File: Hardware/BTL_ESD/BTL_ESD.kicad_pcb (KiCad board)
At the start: 2 copper layers, 73.5 x 92.9 mm, 146 parts, among them J1 DC-005-5A-2.0, J2 BOOT, J3 Load Program, J4 Socket_TFT_1, J5 Socket_TFT_2, J6 USB_B_Micro, J7 220VAC, K1 SRD-05VDC-SL-C, Q1 MMBT2222A, Q2 MMBT2222A, Q3 MMBT2222A, Q4 MMBT2222A, SW1 MS-22D18G2ROHS, SW2 RESET, SW3 ENABLE, SW4 FLASH, U1 ICL7662CBA-T, U2 AMS1117-3.3, U3 TPS54331D, U4 STM32F103RCTx, U5 ESP32-WROOM-32E__4MB_HIGH_TEM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, U6 MCP6002-E_SN, U7 INA128UA, U8 CH340C, U9 PC817, Y1 8MHz, Y2 32.768KHz

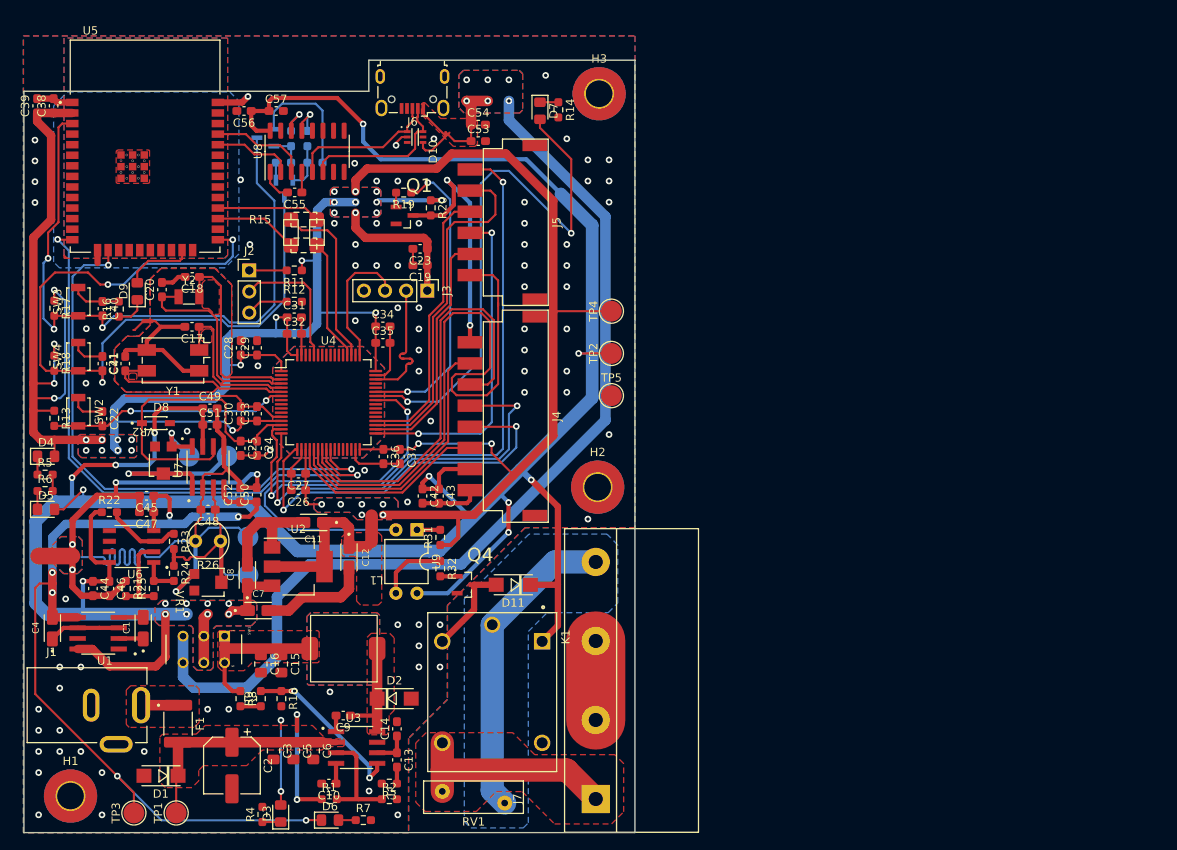
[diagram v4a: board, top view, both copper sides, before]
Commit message: code:ESP32: update uart driver, main.c && hardware file pcb
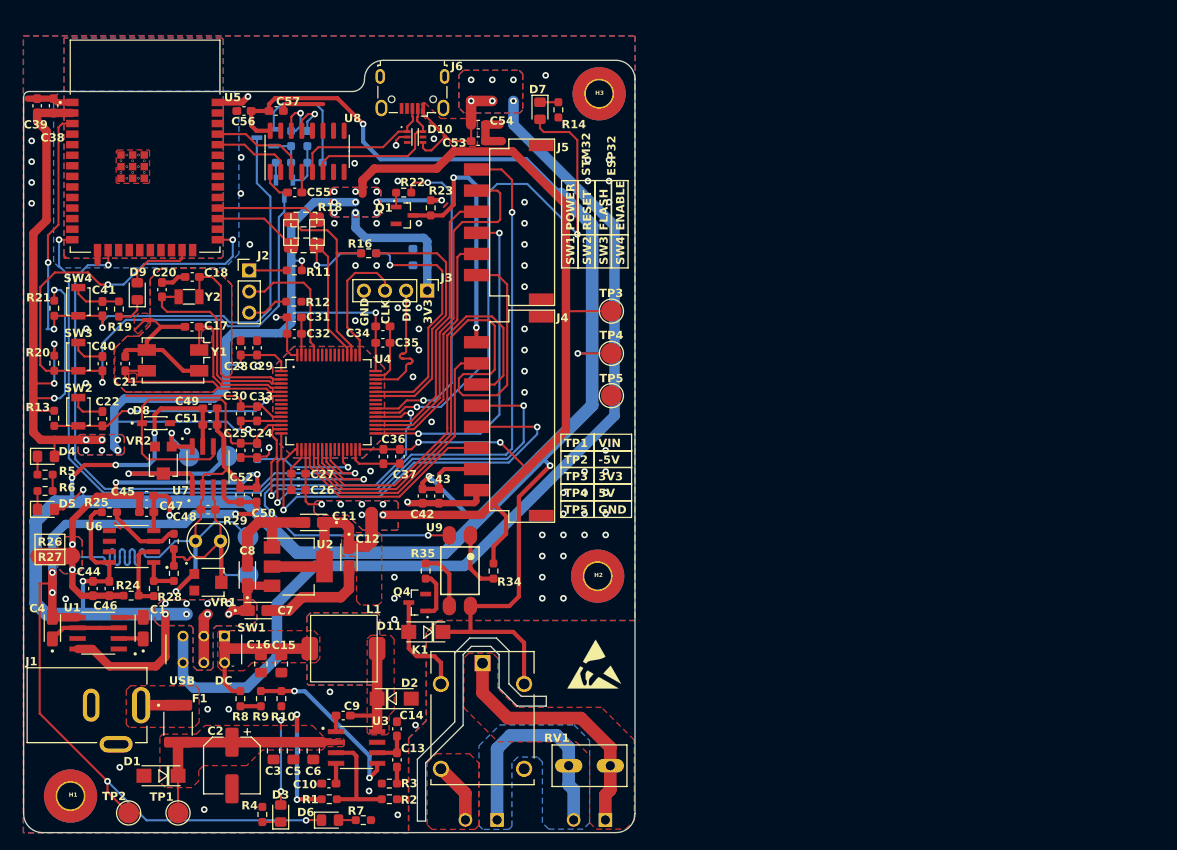
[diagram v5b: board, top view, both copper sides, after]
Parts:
- removed J7: 220VAC, HB9500:HB9500_9_5_4P
- added R15: 0/1%, Resistor_SMD:R_0603_1608Metric_Pad0.98x0.95mm_HandSolder, B.Cu at (139.1, 67.7)
- added R16: 0/1%, Resistor_SMD:R_0603_1608Metric_Pad0.98x0.95mm_HandSolder, F.Cu at (139.1, 67.7)
- added R17: 10k/1%, Resistor_SMD:R_0603_1608Metric_Pad0.98x0.95mm_HandSolder, B.Cu at (125.8, 91.6)
- added REF**: ESD-Logo_6.6x6mm_SilkScreen, Symbol:ESD-Logo_6.6x6mm_SilkScreen, F.Cu at (166.3, 117.1)
- added REF**: ESD-Logo_6.6x6mm_SilkScreen, Symbol:ESD-Logo_6.6x6mm_SilkScreen, B.Cu at (152.8, 127.5)
- added XA1: LED, MKDS1_2-3:PHOENIX_MKDS1_2-3.81, F.Cu at (152.7, 135.9)
- added XA2: 220VAC, MKDS1_2-3:PHOENIX_MKDS1_2-3.81, F.Cu at (165.7, 135.9)
- C19, C23: moved to B.Cu
- K1: value SRD-05VDC-SL-C -> SRA-05VDC-CL; footprint SRD-05VDC-SL-C:RELAY_SRD-05VDC-SL-C -> SRA-05VDC-CL:RELAY_SRA-05VDC-CL
- RV1: value 470V -> MOV-07D471K; footprint Varistor:RV_Disc_D12mm_W3.9mm_P7.5mm -> MOV-14D471K:MOV07D471K
- U9: value PC817 -> PC817X2NIPW; footprint Package_DIP:DIP-4_W7.62mm -> PC817X2NIP0F:SOT254P975X400-4N
- moved RV1 18.0 mm to (165.7, 129.3)
- moved D11 11.9 mm to (146.0, 113.3)
- moved H2 10.7 mm to (166.7, 106.6)
- moved R34 7.57 mm to (154.2, 105.9), turned to -90 degrees
- moved U9 7.12 mm to (150.1, 105.9)
- moved Q4 6.20 mm to (145.0, 109.7), turned to 180 degrees
- moved K1 3.34 mm to (152.8, 123.6)
- moved R35 1.77 mm to (146.0, 105.9)
- moved R24 1.06 mm to (110.6, 108.9), turned to 0 degrees
- moved J4 0.76 mm to (153.7, 87.3)
- moved J5 0.76 mm to (153.7, 64.0)
- moved TP2 0.64 mm to (110.3, 135.0)
- moved C24 0.25 mm to (125.7, 91.4)
- moved C25 0.25 mm to (123.8, 91.4)
- moved TP1 0.23 mm to (116.2, 135.0)
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- renumbered C41 to C40, C40 to C41, R15 to R18, R16 to R19, R18 to R20, R17 to R21, R19 to R22, R20 to R23, R21 to R24, R22 to R25, R23 to R26, R24 to R27, R25 to R28, R26 to R29, R27 to R30, R28 to R31, R29 to R32, R30 to R33, R31 to R34, R32 to R35, SW4 to SW3, SW3 to SW4, TP3 to TP2, TP4 to TP3, TP2 to TP4
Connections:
- net /STM32/BOOT renamed /STM32/BOOT0
- K1 pad NO: Net-(J7-Pin_1) -> Net-(K1-PadNO)
- RV1 pad 1: Net-(J7-Pin_1) -> Net-(RV1-Pad1)
- U4 pad 28: unconnected-(U4-PB2-Pad28) -> Net-(U4-PB2)
- U4 pad 37: unconnected-(U4-PC6-Pad37) -> CONTROL_LED
- U4 pad 38: unconnected-(U4-PC7-Pad38) -> /STM32/LED_TEST
- U4 pad 39: unconnected-(U4-PC8-Pad39) -> TFT_BL
- U4 pad 41: CONTROL_LED -> unconnected-(U4-PA8-Pad41)
- U4 pad 42: /STM32/LED_TEST -> Net-(U4-PA9)
- U4 pad 43: TFT_BL -> Net-(U4-PA10)
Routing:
- net Net-(U4-PA9): track 0.00 -> 31.2 mm
- net Net-(U4-PA10): track 0.00 -> 30.0 mm, vias 0 -> 1
- net Net-(RV1-Pad1): track 0.00 -> 27.4 mm
- net Net-(J7-Pin_1): track 25.7 -> 0.00 mm
- net GND: track 126.5 -> 141.6 mm, vias 83 -> 77
- net Net-(U4-PB2): track 0.00 -> 13.7 mm, vias 0 -> 1
- net Net-(J7-Pin_2): track 9.50 -> 0.00 mm
- net UART4_RX: track 14.7 -> 23.0 mm, vias 0 -> 1
- net +3V3: track 369.2 -> 377.1 mm, vias 35 -> 33
- net Net-(K1-PadNO): track 0.00 -> 7.36 mm
- net Net-(K1-PadCOM): track 37.6 -> 30.6 mm
- net CONTROL_LED: track 47.0 -> 53.7 mm, vias 1 -> 2
- net Net-(U9-A): track 2.79 -> 7.26 mm
- net Net-(Q4-Pad1): track 2.03 -> 5.89 mm
- net TFT_BL: track 36.3 -> 39.7 mm
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- added copper zone on F.Cu, net Net-(K1-PadCOM)
- added copper zone on F.Cu, net Net-(K1-PadNO)
- added copper zone on B.Cu, net Net-(RV1-Pad1)
- removed copper zone on F.Cu, net Net-(J7-Pin_1)
- removed copper zone on B.Cu, net Net-(K1-PadCOM)
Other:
- board size 73.5 x 92.9 mm -> 73.5 x 92.8 mm
- board text added: "-5V"
- board text added: "220VAC"
- board text added: "3V3"
- board text added: "5V"
- board text added: "CLK"
- board text added: "DC"
- board text added: "DIO"
- board text added: "ENABLE"
- board text added: "ESP32"
- board text added: "FLASH"
- board text added: "GND"
- board text added: "LED"
- board text added: "POWER"
- board text added: "RESET"
- board text added: "RG"
- board text added: "STM32"
- board text added: "SW1"
- board text added: "SW2"
- board text added: "SW3"
- board text added: "SW4"
- board text added: "TP1"
- board text added: "TP2"
- board text added: "TP3"
- board text added: "TP4"
- board text added: "TP5"
- board text added: "TP6"
- board text added: "TP7"
- board text added: "TP8"
- board text added: "TP9"
- board text added: "USB"
- board text added: "VG1"
- board text added: "VIN"

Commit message: folder:firmware: add calib adc, adc driver, illuminance
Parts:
- R1: value 330k/1% -> 100k/1%
- R2: value 47k/1% -> 20k/1%

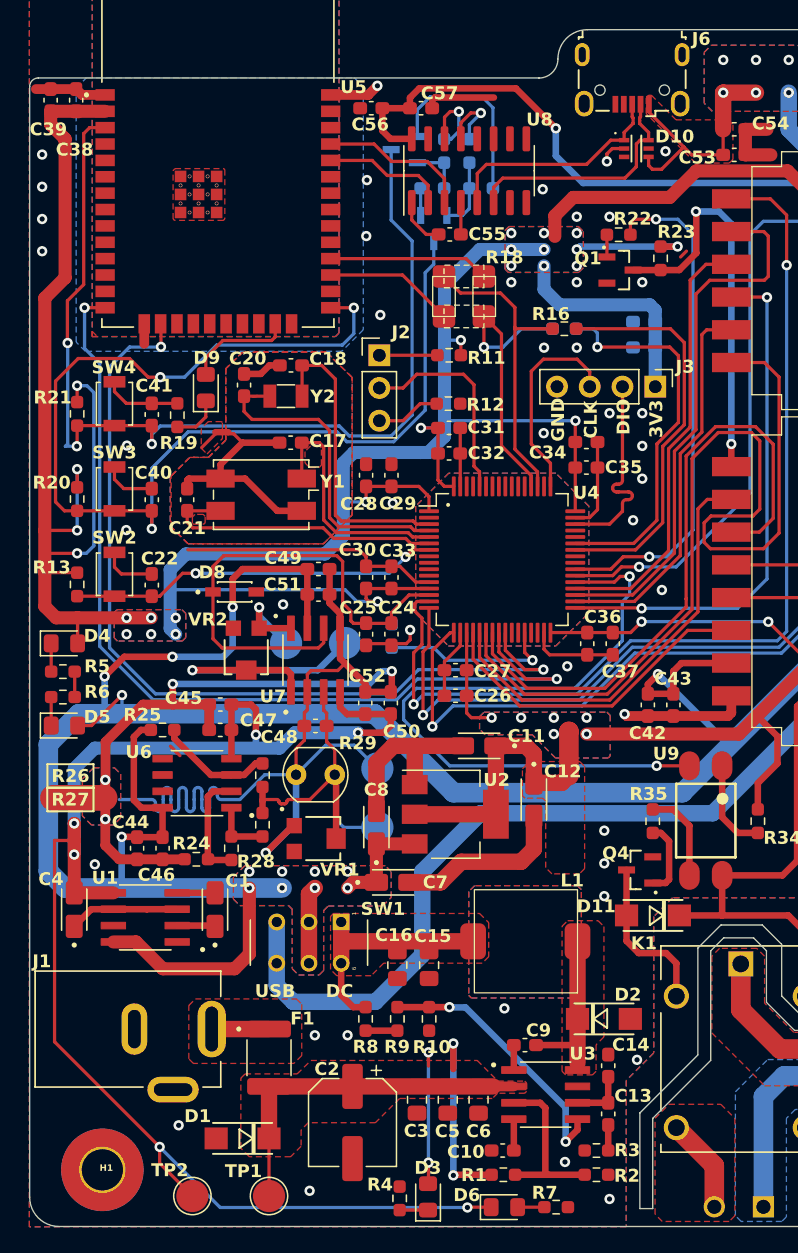
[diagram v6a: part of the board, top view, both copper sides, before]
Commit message: code:esp32:update main
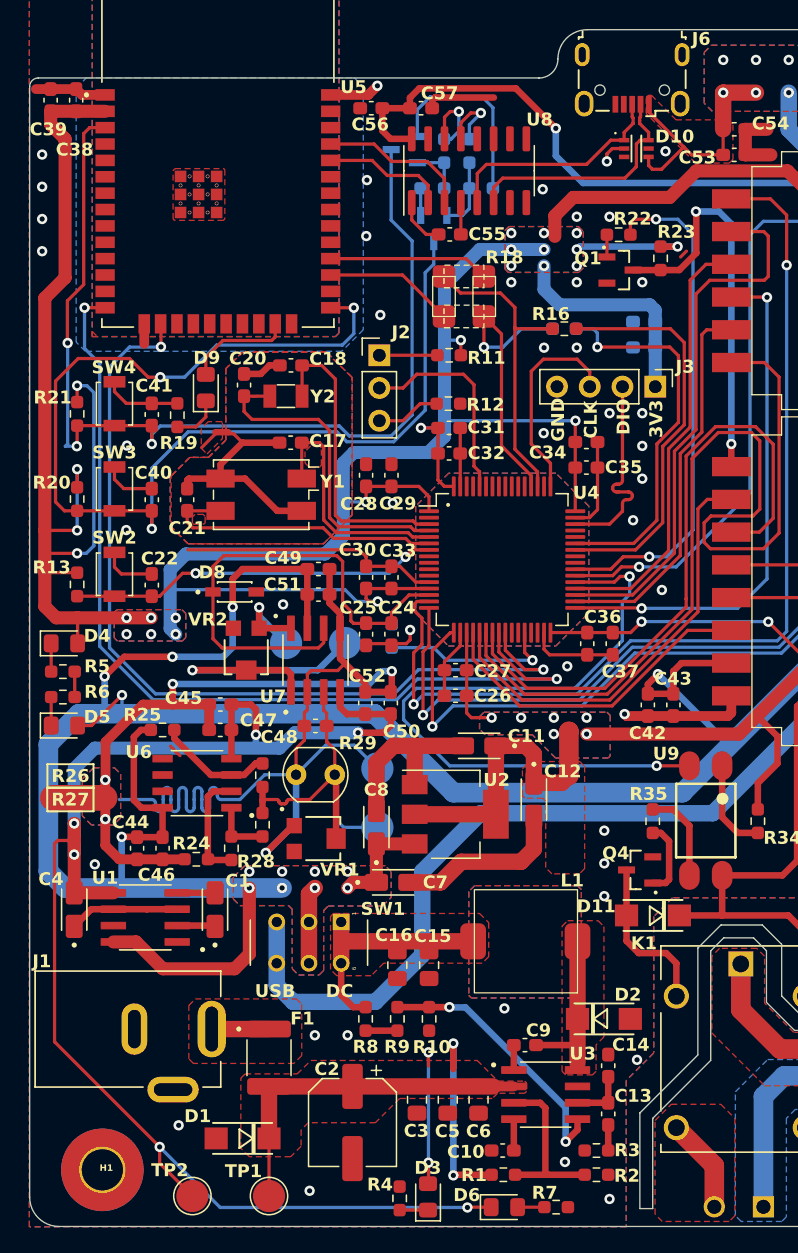
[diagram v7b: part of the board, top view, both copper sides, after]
